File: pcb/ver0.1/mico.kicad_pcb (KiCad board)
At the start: 2 copper layers, 30 x 138 mm, 41 parts, among them J1 USB_A, J2 SWD Prog, U1 MCP1702, U2 MP23DB01HPTR, U3 W25Q128JV, U4 RP2040, U5 logo, Y1 H130B-12.000-20-3050-EXT-TR

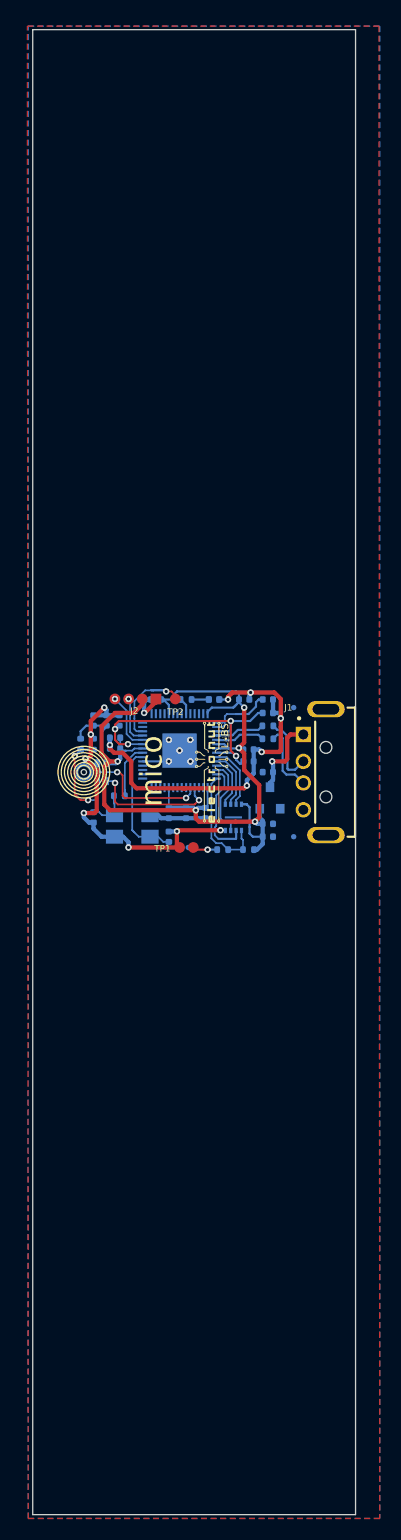
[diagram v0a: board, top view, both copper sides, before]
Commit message: precisely place microphones, seperate each mic resistor and capacitors
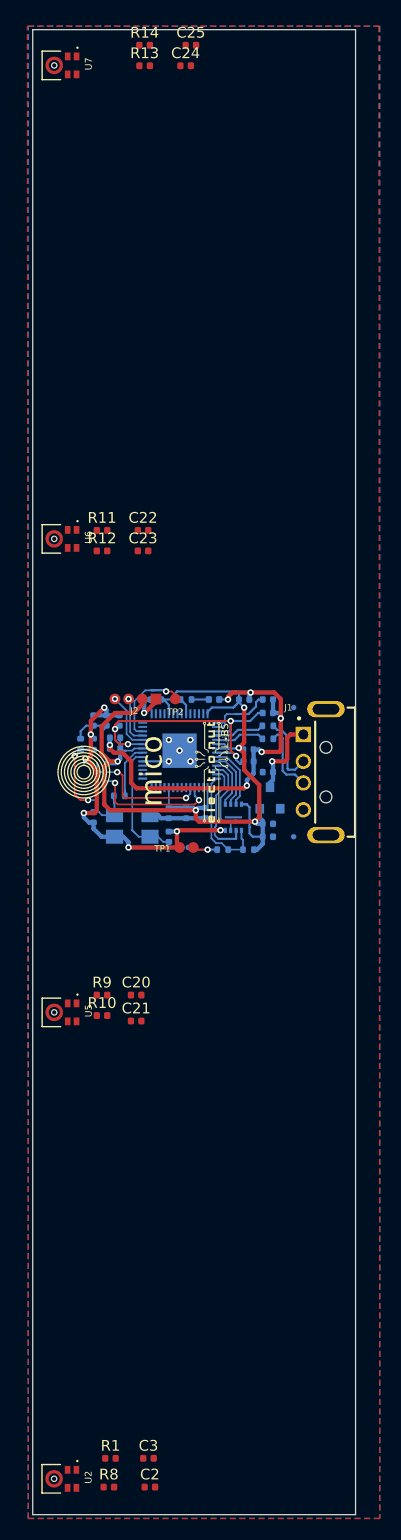
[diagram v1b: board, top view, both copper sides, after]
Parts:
- added C2: 0.1uF, Capacitor_SMD:C_0402_1005Metric, F.Cu at (127.6, 178.4)
- added C20: 0.1uF, Capacitor_SMD:C_0402_1005Metric, F.Cu at (126.4, 132.7)
- added C21: 1uF, Capacitor_SMD:C_0402_1005Metric, F.Cu at (126.4, 135.1)
- added C22: 0.1uF, Capacitor_SMD:C_0402_1005Metric, F.Cu at (127.0, 89.5)
- added C23: 1uF, Capacitor_SMD:C_0402_1005Metric, F.Cu at (127.0, 91.4)
- added C24: 0.1uF, Capacitor_SMD:C_0402_1005Metric, F.Cu at (131.0, 46.4)
- added C25: 1uF, Capacitor_SMD:C_0402_1005Metric, F.Cu at (131.4, 44.5)
- added C3: 1uF, Capacitor_SMD:C_0402_1005Metric, F.Cu at (127.5, 175.8)
- added R1: 10K, Resistor_SMD:R_0402_1005Metric, F.Cu at (124.0, 175.8)
- added R10: 10K, Resistor_SMD:R_0402_1005Metric, F.Cu at (123.2, 134.6)
- added R11: 10K, Resistor_SMD:R_0402_1005Metric, F.Cu at (123.2, 89.5)
- added R12: 10K, Resistor_SMD:R_0402_1005Metric, F.Cu at (123.2, 91.4)
- added R13: 10K, Resistor_SMD:R_0402_1005Metric, F.Cu at (127.2, 46.4)
- added R14: 10K, Resistor_SMD:R_0402_1005Metric, F.Cu at (127.2, 44.5)
- added R8: 10K, Resistor_SMD:R_0402_1005Metric, F.Cu at (123.8, 178.4)
- added R9: 10K, Resistor_SMD:R_0402_1005Metric, F.Cu at (123.2, 132.7)
- added U5: MP23DB01HPTR, mico:MIC_SPH0641LU4H-1, F.Cu at (118.8, 134.3)
- added U6: MP23DB01HPTR, mico:MIC_SPH0641LU4H-1, F.Cu at (118.8, 90.3)
- added U7: MP23DB01HPTR, mico:MIC_SPH0641LU4H-1, F.Cu at (118.8, 46.3)
- U2: moved to F.Cu
- moved U2 65.7 mm to (118.7, 177.7), turned to 270 degrees
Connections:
- net /MIC_DOUT renamed /MIC_DOUT_0
- U4 pad 11: (no net) -> Net-(U4-Pad11)
- U4 pad 12: (no net) -> Net-(U4-Pad12)
- U4 pad 13: (no net) -> Net-(U4-Pad13)
- U4 pad 14: (no net) -> Net-(U4-Pad14)
- U4 pad 15: (no net) -> Net-(U4-Pad15)
- U4 pad 16: (no net) -> Net-(U4-Pad16)
- U4 pad 17: (no net) -> Net-(U4-Pad17)
- U4 pad 18: (no net) -> Net-(U4-Pad18)
- U4 pad 2: (no net) -> Net-(U4-Pad2)
- U4 pad 27: (no net) -> Net-(U4-Pad27)
- U4 pad 28: (no net) -> Net-(U4-Pad28)
- U4 pad 29: (no net) -> Net-(U4-Pad29)
- U4 pad 3: (no net) -> Net-(U4-Pad3)
- U4 pad 30: (no net) -> Net-(U4-Pad30)
- U4 pad 31: (no net) -> Net-(U4-Pad31)
- U4 pad 32: (no net) -> Net-(U4-Pad32)
- U4 pad 34: (no net) -> Net-(U4-Pad34)
- U4 pad 35: (no net) -> Net-(U4-Pad35)
- U4 pad 36: (no net) -> Net-(U4-Pad36)
- U4 pad 38: (no net) -> Net-(U4-Pad38)
- U4 pad 39: (no net) -> Net-(U4-Pad39)
- U4 pad 40: (no net) -> Net-(U4-Pad40)
- U4 pad 41: (no net) -> Net-(U4-Pad41)
- U4 pad 6: (no net) -> /MIC_DOUT_1
- U4 pad 7: (no net) -> /MIC_DOUT_2
- U4 pad 8: (no net) -> /MIC_DOUT_3
- U4 pad 9: (no net) -> Net-(U4-Pad9)

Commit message: wire up mics, just need to connect data lines
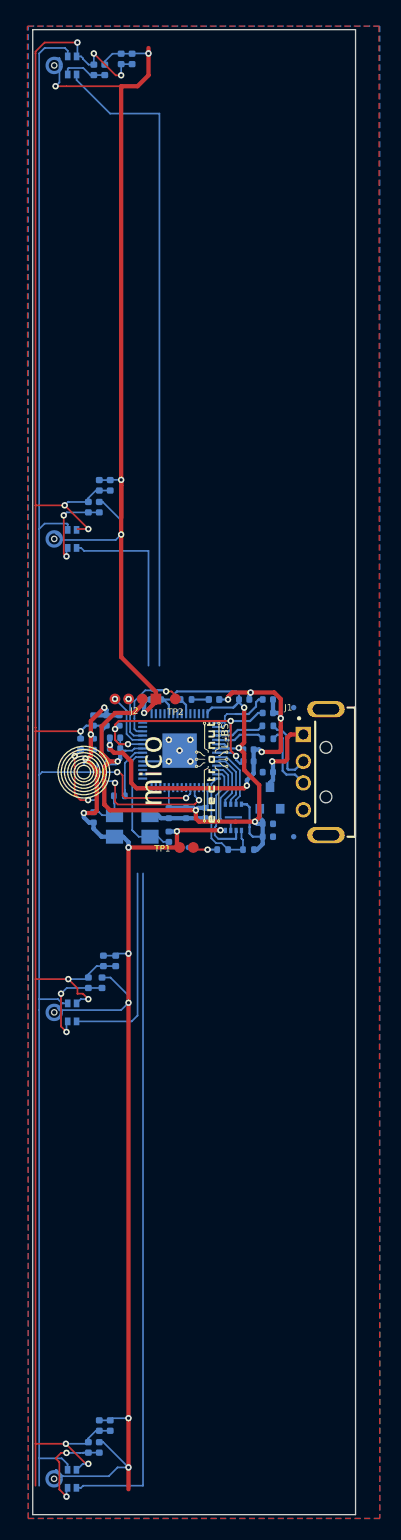
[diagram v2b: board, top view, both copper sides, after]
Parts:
- C2, C20, C21, C22, C23, C24, C25, C3, R1, R10, R11, R12, R13, R14, R8, R9, U2, U5, U6, U7: moved to B.Cu
- moved C23 6.82 mm to (124.0, 85.3), turned to 270 degrees
- moved C2 6.80 mm to (124.0, 172.7), turned to 270 degrees
- moved C25 6.60 mm to (125.0, 45.7), turned to 270 degrees
- moved C21 5.90 mm to (124.5, 129.5), turned to 270 degrees
- moved C22 5.84 mm to (122.9, 85.3), turned to 270 degrees
- moved C3 5.49 mm to (122.9, 172.7), turned to 270 degrees
- moved C24 5.02 mm to (126.0, 45.7), turned to 270 degrees
- moved R13 4.74 mm to (122.4, 46.7), turned to 270 degrees
- moved C20 4.40 mm to (123.3, 129.5), turned to 270 degrees
- moved R14 4.35 mm to (123.4, 46.7), turned to 90 degrees
- moved R12 4.07 mm to (122.9, 87.4), turned to 90 degrees
- moved R8 3.79 mm to (122.9, 174.8), turned to 90 degrees
- moved R10 3.05 mm to (123.2, 131.6), turned to 90 degrees
- moved R11 2.50 mm to (121.9, 87.4), turned to 270 degrees
- moved R1 2.29 mm to (121.9, 174.8), turned to 270 degrees
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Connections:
- R1 pad 2: /MIC_L\R -> Net-(R1-Pad2)
- R10 pad 1: /MIC_L\R -> Net-(R10-Pad1)
- R11 pad 2: /MIC_L\R -> Net-(R11-Pad2)
- R12 pad 1: /MIC_L\R -> Net-(R11-Pad2)
- R13 pad 2: /MIC_L\R -> Net-(R13-Pad2)
- R14 pad 1: /MIC_L\R -> Net-(R13-Pad2)
- R8 pad 1: /MIC_L\R -> Net-(R1-Pad2)
- R9 pad 2: /MIC_L\R -> Net-(R10-Pad1)
- U2 pad 2: /MIC_L\R -> Net-(R1-Pad2)
- U5 pad 2: /MIC_L\R -> Net-(R10-Pad1)
- U6 pad 2: /MIC_L\R -> Net-(R11-Pad2)
- U7 pad 2: /MIC_L\R -> Net-(R13-Pad2)
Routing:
- net +3V3: track 97.6 -> 285.1 mm, vias 5 -> 15
- net GND: track 85.2 -> 266.1 mm, vias 19 -> 27
- net /MIC_CLK: track 12.2 -> 164.2 mm
- net /MIC_DOUT_0: track 12.1 -> 75.2 mm
- net /MIC_DOUT_3: track 0.00 -> 60.8 mm
- net /MIC_DOUT_1: track 0.00 -> 19.1 mm
- net /MIC_DOUT_2: track 0.00 -> 17.5 mm
- net Net-(R1-Pad2): track 0.00 -> 9.44 mm, vias 0 -> 2
- net Net-(R10-Pad1): track 0.00 -> 8.83 mm, vias 0 -> 2
- net Net-(R11-Pad2): track 0.00 -> 8.16 mm, vias 0 -> 2
- net Net-(R13-Pad2): track 0.00 -> 4.27 mm

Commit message: completed pcb layout
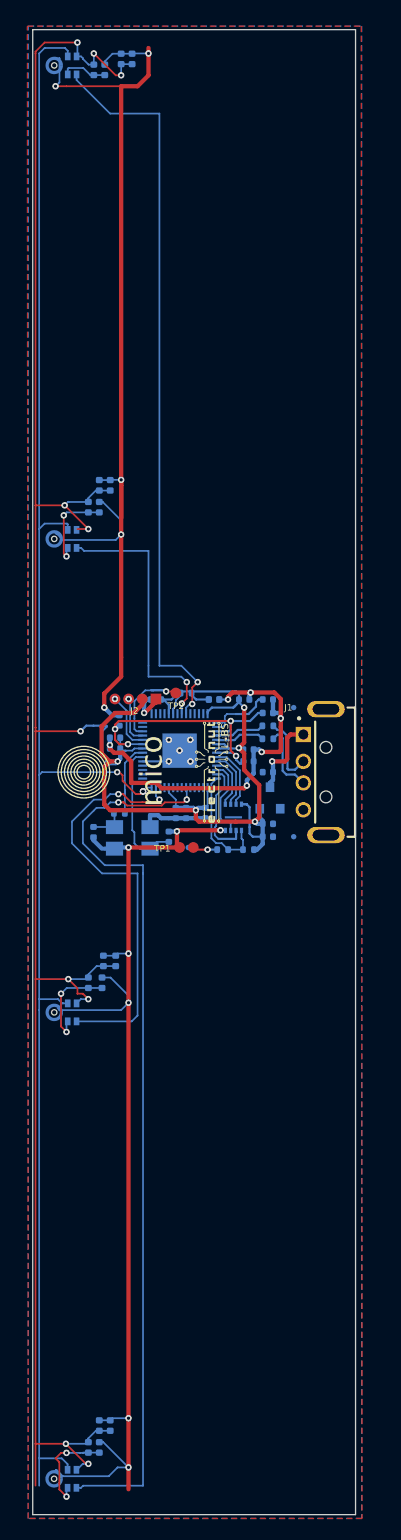
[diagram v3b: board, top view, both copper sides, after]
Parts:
- removed the C2 at (122.4, 107.2)
- removed the C3 at (123.6, 107.2)
- removed the R1 at (122.4, 109.4)
- removed the R8 at (121.2, 109.4)
- moved R7 1.62 mm to (124.8, 115.8)
- moved C19 1.37 mm to (122.4, 117.6)
- moved Y1 1.11 mm to (126.0, 118.1)
- moved C10 0.65 mm to (130.0, 115.8)
- moved R6 0.60 mm to (131.0, 104.6)
- moved TP2 0.55 mm to (130.0, 104.6)
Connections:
- U4 pad 13: Net-(U4-Pad13) -> /MIC_DOUT_1
- U4 pad 14: Net-(U4-Pad14) -> /MIC_CLK
- U4 pad 34: Net-(U4-Pad34) -> /RED_LED
- U4 pad 36: Net-(U4-Pad36) -> /MIC_DOUT_2
- U4 pad 37: /RED_LED -> /MIC_DOUT_3
- U4 pad 4: /MIC_DOUT_0 -> Net-(U4-Pad4)
- U4 pad 5: /MIC_CLK -> Net-(U4-Pad5)
- U4 pad 6: /MIC_DOUT_1 -> /MIC_DOUT_0
- U4 pad 7: /MIC_DOUT_2 -> Net-(U4-Pad7)
- U4 pad 8: /MIC_DOUT_3 -> Net-(U4-Pad8)
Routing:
- net /MIC_DOUT_1: track 19.1 -> 39.2 mm, vias 0 -> 2
- net GND: track 266.1 -> 250.3 mm, vias 27 -> 24
- net /MIC_L\R: track 10.1 -> 0.00 mm, vias 2 -> 0
- net /MIC_DOUT_0: track 75.2 -> 84.6 mm
- net /MIC_DOUT_2: track 17.5 -> 25.7 mm, vias 0 -> 2
- net /MIC_DOUT_3: track 60.8 -> 68.5 mm, vias 0 -> 2
- net /MIC_CLK: track 164.2 -> 158.2 mm, vias 2 -> 3
- net /XOUT: track 5.40 -> 7.03 mm
- net +3V3: track 285.1 -> 284.1 mm
- net /XIN: track 11.7 -> 12.5 mm
- net Net-(C19-Pad2): track 3.89 -> 3.27 mm

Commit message: last few changes, fix DRC issues, generate gerbers
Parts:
- removed the U5 at (133.4, 112.0)
- moved R7 0.13 mm to (124.8, 115.7)
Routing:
- net +3V3: track 284.1 -> 284.8 mm
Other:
- board size 30 x 138 mm -> 30.5 x 138 mm
- rule pad_to_mask_clearance: 0 -> 0.05
- rule trace_min: 0.15 -> 0.127
- rule via_min_drill: 0.3 -> 0.2
- rule via_min_size: 0.2 -> 0.13
- board text added: "MSA"
- board text added: "Multi-Speaker Voice Recognition Array"
- board text removed: "mico"

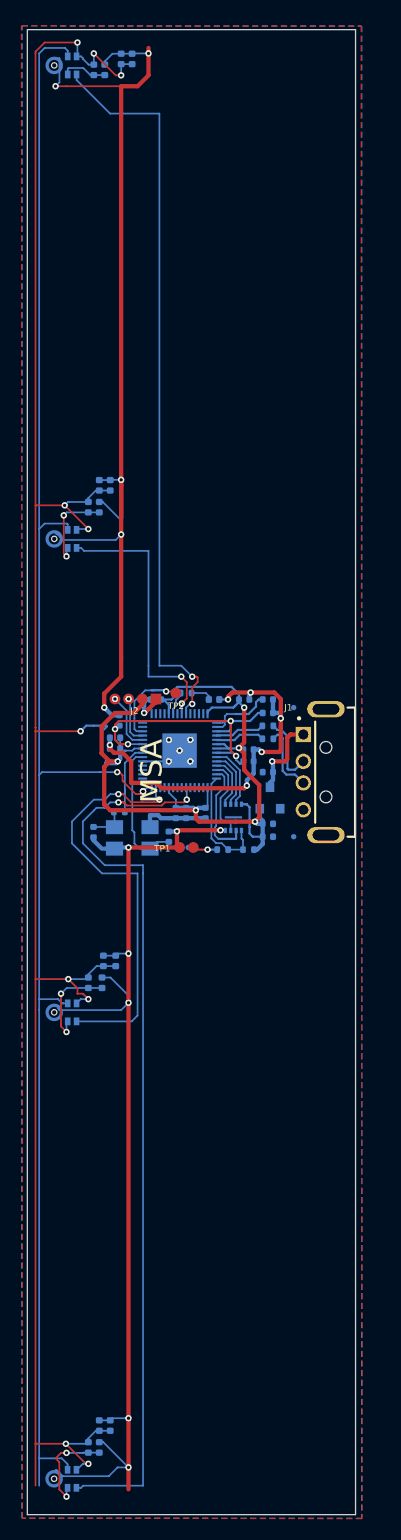
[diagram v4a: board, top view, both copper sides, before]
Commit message: add test pads, last check before order PCB
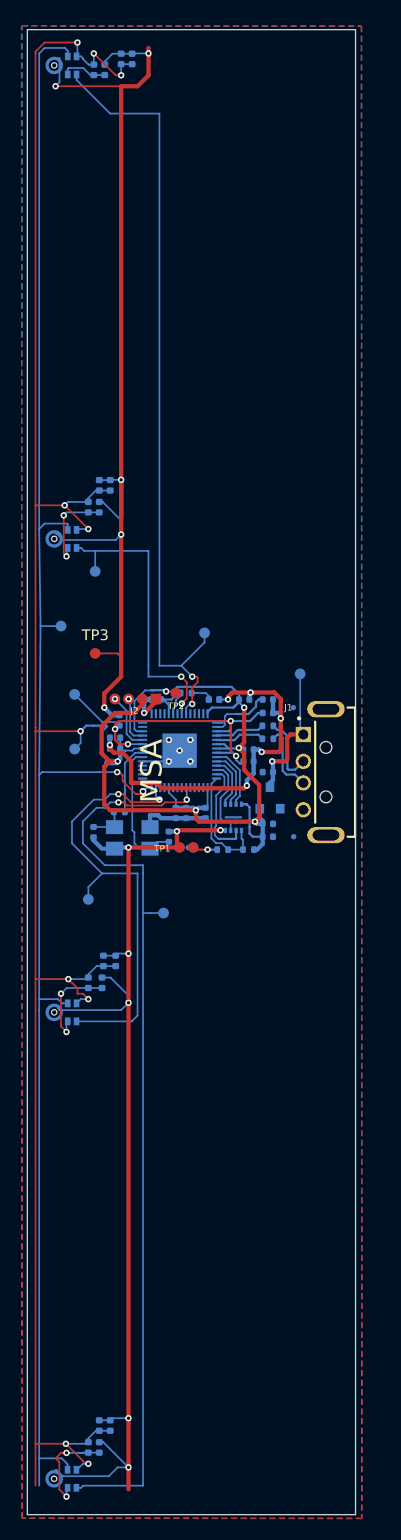
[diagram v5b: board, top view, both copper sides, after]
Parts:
- added TP10: TestPoint, mico:SMD_1x01_P1.27mm, B.Cu at (122.6, 93.3)
- added TP11: TestPoint, mico:SMD_1x01_P1.27mm, B.Cu at (132.7, 99.1)
- added TP3: TestPoint, mico:SMD_1x01_P1.27mm, F.Cu at (122.6, 101.0)
- added TP4: TestPoint, mico:SMD_1x01_P1.27mm, B.Cu at (141.6, 102.9)
- added TP5: TestPoint, mico:SMD_1x01_P1.27mm, B.Cu at (120.7, 109.9)
- added TP6: TestPoint, mico:SMD_1x01_P1.27mm, B.Cu at (120.7, 104.8)
- added TP7: TestPoint, mico:SMD_1x01_P1.27mm, B.Cu at (128.9, 125.1)
- added TP8: TestPoint, mico:SMD_1x01_P1.27mm, B.Cu at (121.9, 123.8)
- added TP9: TestPoint, mico:SMD_1x01_P1.27mm, B.Cu at (119.4, 98.4)
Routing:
- net VBUS: track 7.66 -> 13.4 mm
- net +1V1: track 27.6 -> 33.1 mm
- net /MIC_DOUT_3: track 68.8 -> 72.7 mm
- net /MIC_DOUT_1: track 39.2 -> 42.2 mm
- net GND: track 250.3 -> 252.8 mm
- net /MIC_CLK: track 158.2 -> 160.1 mm
- net /MIC_DOUT_2: track 25.7 -> 27.6 mm
- net /MIC_DOUT_0: track 84.6 -> 86.5 mm
- net +3V3: track 284.8 -> 286.6 mm
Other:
- board text added: "Multi-Speaker Speech Recognition Array"
- board text removed: "Multi-Speaker Voice Recognition Array"

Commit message: add slimstack receptacle to library, add to main rigid board
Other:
- net class Default removed
- net class Diff_pair removed
